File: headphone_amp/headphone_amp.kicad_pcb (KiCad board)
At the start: 2 copper layers, 40 parts, among them J1 Molex_SL_01x02_Male, J2 Molex_SL_01x02_Male, J3 Molex_SL_01x03_Male, J4 Molex_SL_01x03_Male, Q1 PZTA42, Q2 PZTA92, Q3 PZTA42, Q4 PZTA92, U1 NE5532

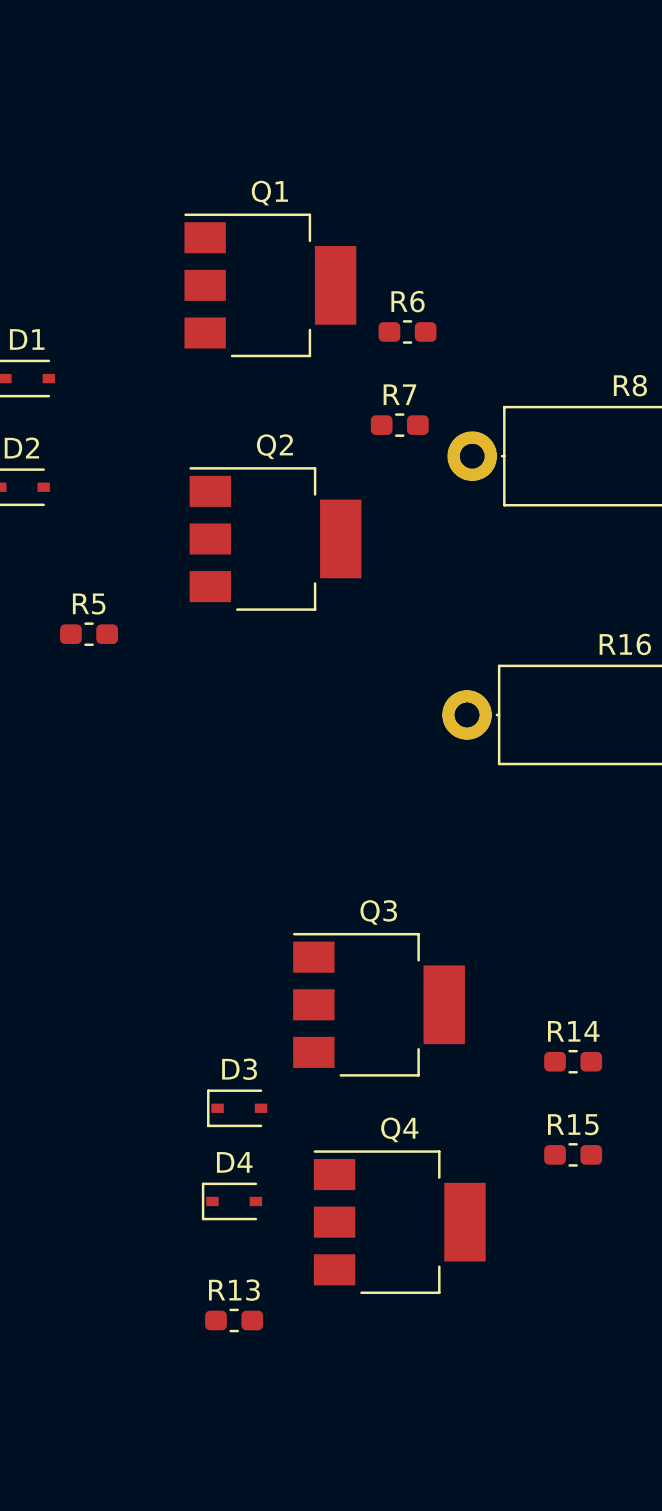
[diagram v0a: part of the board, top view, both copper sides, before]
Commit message: update output transistor symbols/footprints
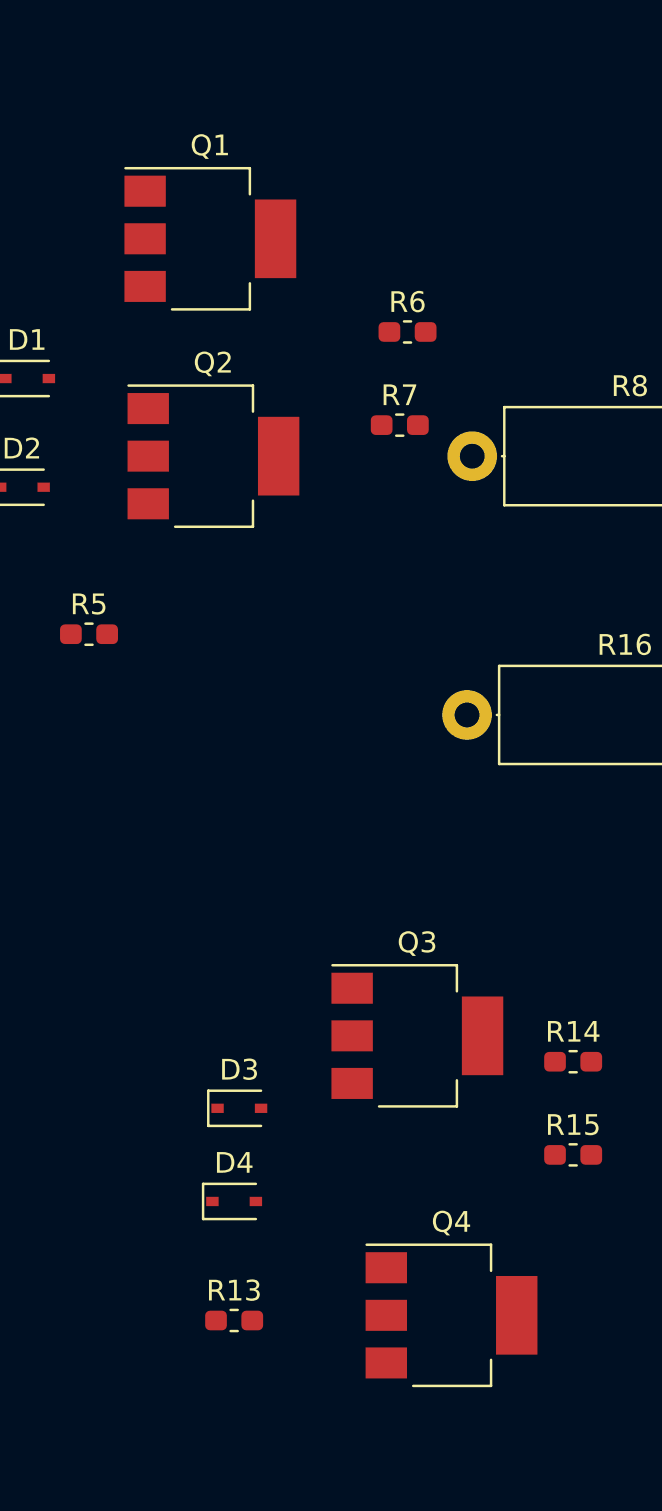
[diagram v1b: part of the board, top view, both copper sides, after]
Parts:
- Q1, Q2, Q3, Q4: footprint Package_TO_SOT_SMD:SOT-223 -> Package_TO_SOT_SMD:SOT-223-3_TabPin2
- moved Q4 5.15 mm to (93.5, 167.0)
- moved Q2 5.00 mm to (82.0, 125.5)
- moved Q1 3.67 mm to (81.8, 115.0)
- moved Q3 2.38 mm to (91.8, 153.5)
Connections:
- Q2 pad 1: Net-(D2-Pad1) -> Net-(Q2-Pad1)
- Q2 pad 2: VEE -> Net-(D2-Pad1)
- Q2 pad 3: Net-(Q2-Pad3) -> VEE
- Q4 pad 1: Net-(D4-Pad1) -> Net-(Q4-Pad1)
- Q4 pad 2: VEE -> Net-(D4-Pad1)
- Q4 pad 3: Net-(Q4-Pad3) -> VEE
- R15 pad 2: Net-(Q4-Pad3) -> Net-(Q4-Pad1)
- R7 pad 2: Net-(Q2-Pad3) -> Net-(Q2-Pad1)

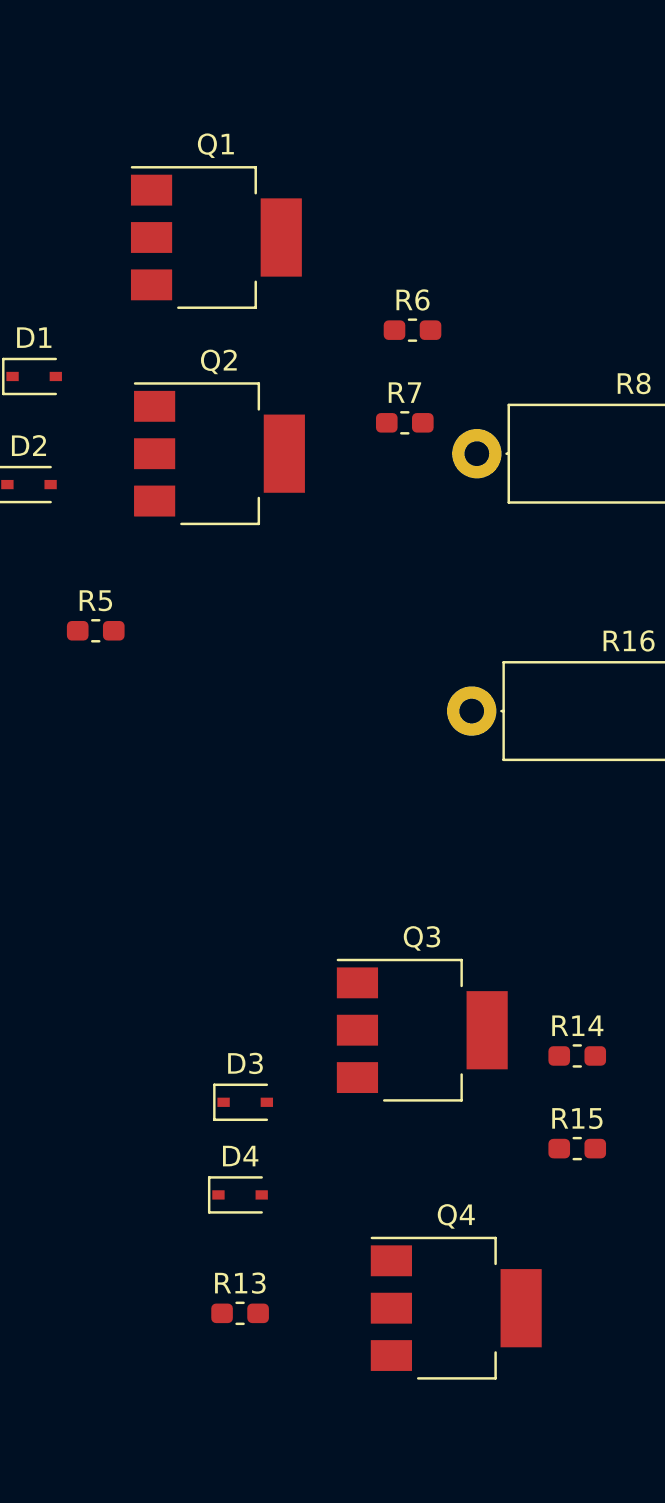
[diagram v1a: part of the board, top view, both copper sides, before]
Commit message: change output transistors to std lib versions (now in upstream)
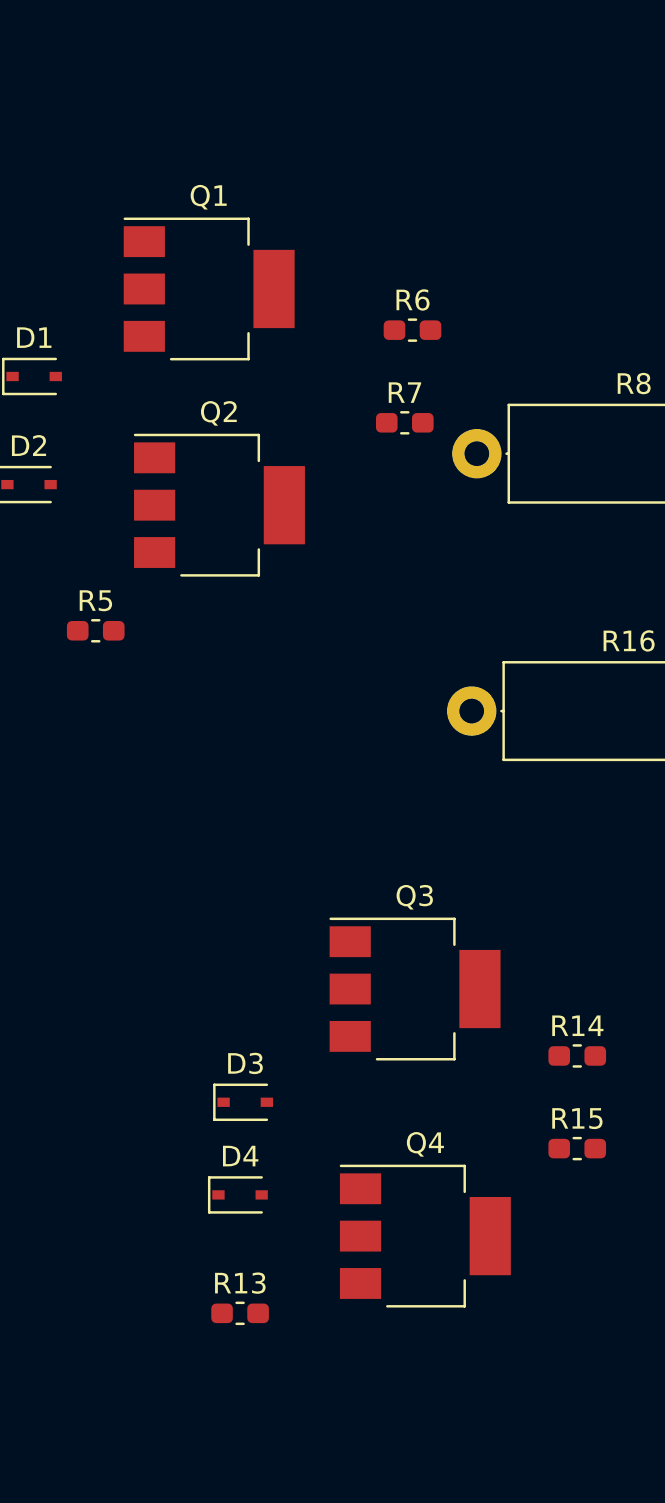
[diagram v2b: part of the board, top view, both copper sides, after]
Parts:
- moved Q4 3.81 mm to (92.0, 163.5)
- moved Q1 2.52 mm to (81.5, 117.5)
- moved Q2 2.50 mm to (82.0, 128.0)
- moved Q3 2.03 mm to (91.5, 151.5)
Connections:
- Q2 pad 1: Net-(Q2-Pad1) -> Net-(D2-Pad1)
- Q2 pad 2: Net-(D2-Pad1) -> VEE
- Q2 pad 3: VEE -> Net-(Q2-Pad3)
- Q4 pad 1: Net-(Q4-Pad1) -> Net-(D4-Pad1)
- Q4 pad 2: Net-(D4-Pad1) -> VEE
- Q4 pad 3: VEE -> Net-(Q4-Pad3)
- R15 pad 2: Net-(Q4-Pad1) -> Net-(Q4-Pad3)
- R7 pad 2: Net-(Q2-Pad1) -> Net-(Q2-Pad3)
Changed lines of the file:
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@@
   (net 24 "Net-(Q1-Pad3)")
   (net 25 "Net-(Q3-Pad3)")
-  (net 26 "Net-(Q2-Pad1)")
-  (net 27 "Net-(Q4-Pad1)")
+  (net 26 "Net-(Q2-Pad3)")
+  (net 27 "Net-(Q4-Pad3)")
   (net_class Default "This is the default net class."
     (clearance 0.2)
@@
     (add_net "Net-(D4-Pad1)")
     (add_net "Net-(Q1-Pad3)")
-    (add_net "Net-(Q2-Pad1)")
+    (add_net "Net-(Q2-Pad3)")
     (add_net "Net-(Q3-Pad3)")
-    (add_net "Net-(Q4-Pad1)")
+    (add_net "Net-(Q4-Pad3)")
     (add_net VCC)
     (add_net VEE)
   )
   (module Package_TO_SOT_SMD:SOT-223-3_TabPin2 (layer F.Cu)
-    (at 93.5 167)
+    (at 92 163.5)
     (descr "module CMS SOT223 4 pins")
     (tags "CMS SOT")
@@
     )
     (pad 1 smd rect (at -3.15 -2.3) (size 2 1.5) (layers F.Cu F.Paste F.Mask)
-      (net 27 "Net-(Q4-Pad1)"))
+      (net 17 "Net-(D4-Pad1)"))
     (pad 3 smd rect (at -3.15 2.3) (size 2 1.5) (layers F.Cu F.Paste F.Mask)
+      (net 27 "Net-(Q4-Pad3)"))
+    (pad 2 smd rect (at -3.15 0) (size 2 1.5) (layers F.Cu F.Paste F.Mask)
       (net 10 VEE))
-    (pad 2 smd rect (at -3.15 0) (size 2 1.5) (layers F.Cu F.Paste F.Mask)
-      (net 17 "Net-(D4-Pad1)"))
     (pad 2 smd rect (at 3.15 0) (size 2 3.8) (layers F.Cu F.Paste F.Mask)
-      (net 17 "Net-(D4-Pad1)"))
+      (net 10 VEE))
     (model ${KISYS3DMOD}/Package_TO_SOT_SMD.3dshapes/SOT-223.wrl
       (at (xyz 0 0 0))
@@
   )
   (module Package_TO_SOT_SMD:SOT-223-3_TabPin2 (layer F.Cu)
-    (at 91.85 153.5)
+    (at 91.5 151.5)
     (descr "module CMS SOT223 4 pins")
     (tags "CMS SOT")
@@
   )
   (module Package_TO_SOT_SMD:SOT-223-3_TabPin2 (layer F.Cu)
-    (at 82 125.5)
+    (at 82 128)
     (descr "module CMS SOT223 4 pins")
     (tags "CMS SOT")
@@
     )
     (pad 1 smd rect (at -3.15 -2.3) (size 2 1.5) (layers F.Cu F.Paste F.Mask)
-      (net 26 "Net-(Q2-Pad1)"))
+      (net 14 "Net-(D2-Pad1)"))
     (pad 3 smd rect (at -3.15 2.3) (size 2 1.5) (layers F.Cu F.Paste F.Mask)
+      (net 26 "Net-(Q2-Pad3)"))
+    (pad 2 smd rect (at -3.15 0) (size 2 1.5) (layers F.Cu F.Paste F.Mask)
       (net 10 VEE))
-    (pad 2 smd rect (at -3.15 0) (size 2 1.5) (layers F.Cu F.Paste F.Mask)
-      (net 14 "Net-(D2-Pad1)"))
     (pad 2 smd rect (at 3.15 0) (size 2 3.8) (layers F.Cu F.Paste F.Mask)
-      (net 14 "Net-(D2-Pad1)"))
+      (net 10 VEE))
     (model ${KISYS3DMOD}/Package_TO_SOT_SMD.3dshapes/SOT-223.wrl
       (at (xyz 0 0 0))
@@
   )
   (module Package_TO_SOT_SMD:SOT-223-3_TabPin2 (layer F.Cu)
-    (at 81.85 115)
+    (at 81.5 117.5)
     (descr "module CMS SOT223 4 pins")
     (tags "CMS SOT")
@@
     (fp_line (start -0.8 0.4) (end -0.8 -0.4) (layer F.Fab) (width 0.1))
     (pad 2 smd roundrect (at 0.875 0) (size 1.05 0.95) (layers F.Cu F.Paste F.Mask) (roundrect_rratio 0.25)
-      (net 27 "Net-(Q4-Pad1)"))
+      (net 27 "Net-(Q4-Pad3)"))
     (pad 1 smd roundrect (at -0.875 0) (size 1.05 0.95) (layers F.Cu F.Paste F.Mask) (roundrect_rratio 0.25)
       (net 7 "Net-(C4-Pad1)"))
@@
     (fp_line (start -0.8 0.4) (end -0.8 -0.4) (layer F.Fab) (width 0.1))
     (pad 2 smd roundrect (at 0.875 0) (size 1.05 0.95) (layers F.Cu F.Paste F.Mask) (roundrect_rratio 0.25)
-      (net 26 "Net-(Q2-Pad1)"))
+      (net 26 "Net-(Q2-Pad3)"))
     (pad 1 smd roundrect (at -0.875 0) (size 1.05 0.95) (layers F.Cu F.Paste F.Mask) (roundrect_rratio 0.25)
       (net 2 "Net-(C1-Pad1)"))

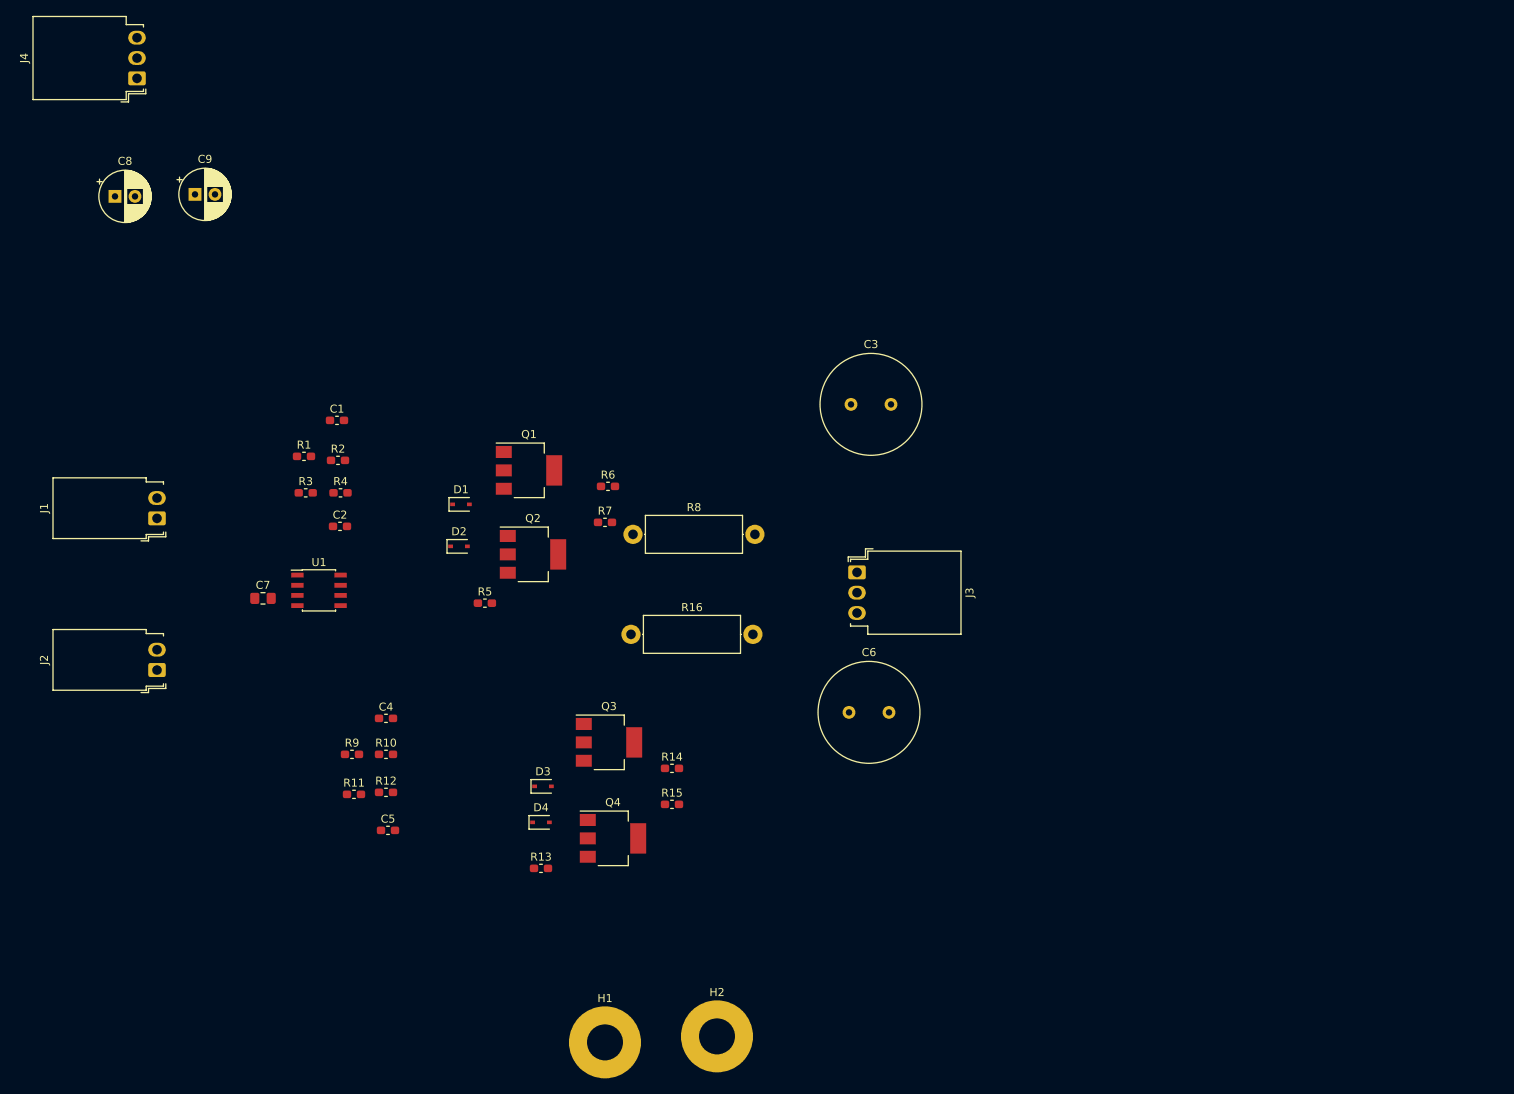
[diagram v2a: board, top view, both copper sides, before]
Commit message: initial layout for headphone amplifier. Still need to finalize mounting orientation and adjust connectors/mounting holes if necessary
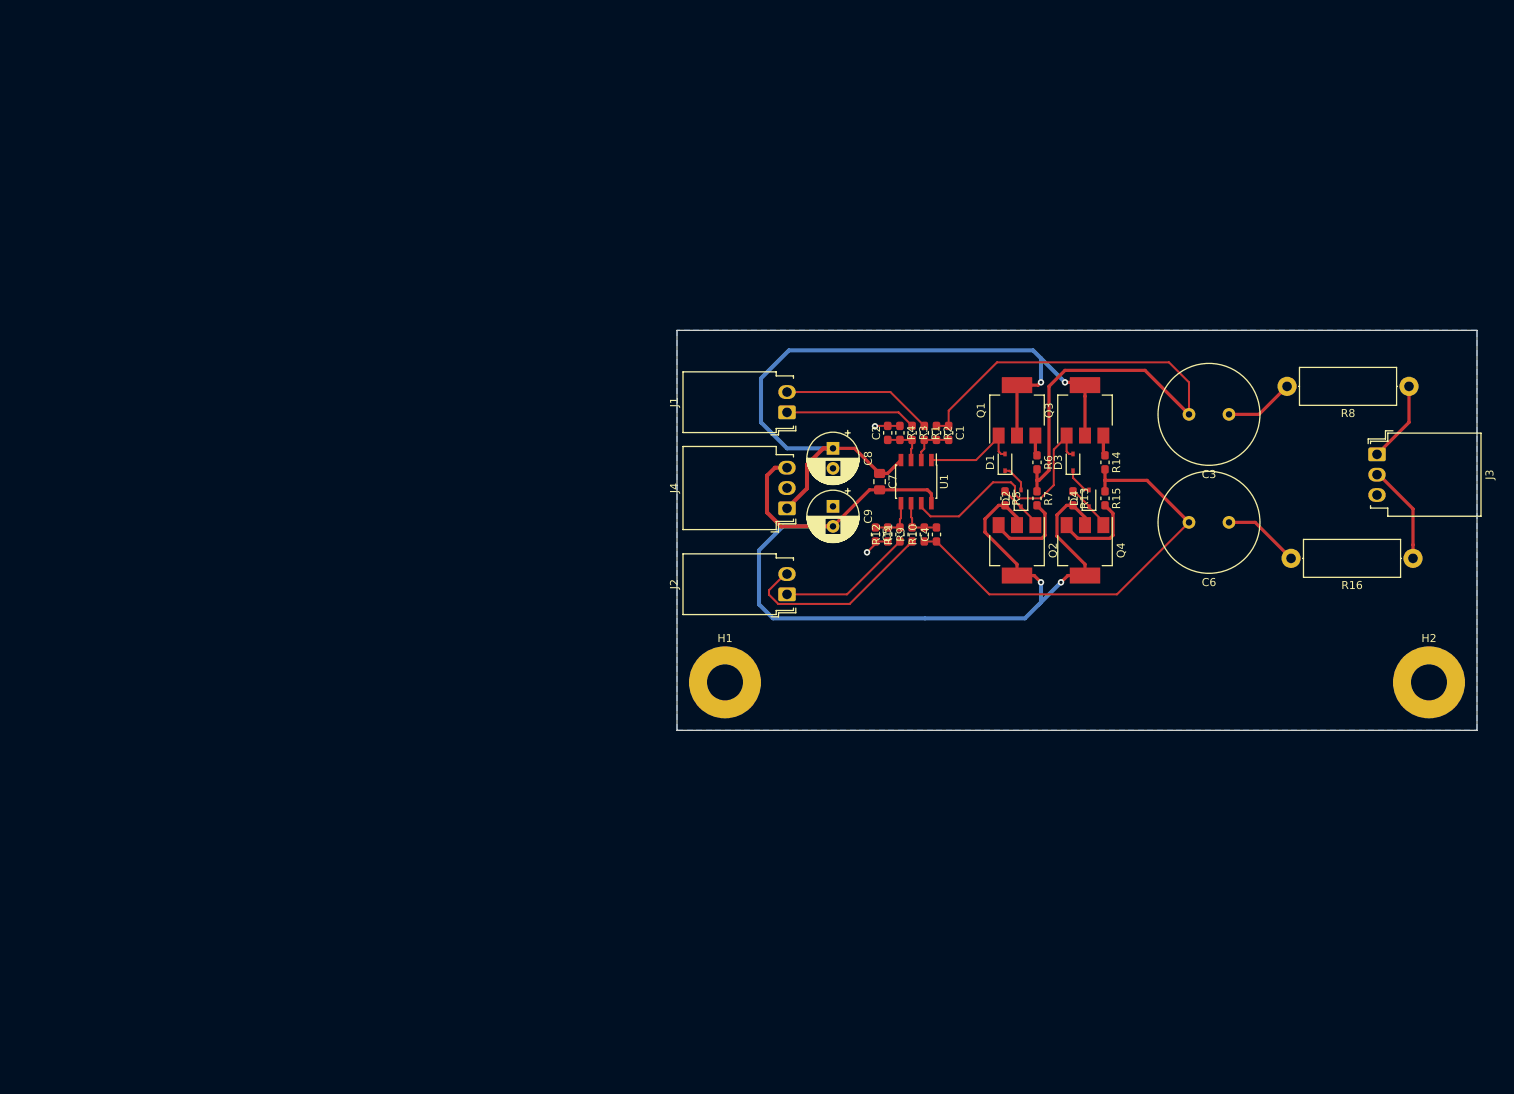
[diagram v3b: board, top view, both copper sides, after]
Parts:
- moved H2 99.4 mm to (194.0, 144.0)
- moved R8 98.7 mm to (191.5, 107.0), turned to 180 degrees
- moved R16 98.2 mm to (192.0, 128.5), turned to 180 degrees
- moved J4 97.4 mm to (113.8, 122.2)
- moved C8 95.1 mm to (119.5, 114.8), turned to 270 degrees
- moved C9 88.8 mm to (119.5, 122.0), turned to 270 degrees
- moved R13 81.0 mm to (149.5, 121.0), turned to 270 degrees
- moved J1 79.9 mm to (113.8, 110.2)
- moved D4 79.6 mm to (151.5, 121.0), turned to 90 degrees
- moved J2 79.3 mm to (113.8, 133.0)
- moved C7 78.4 mm to (125.3, 118.9), turned to 270 degrees
- moved D3 77.6 mm to (149.5, 116.5), turned to 90 degrees
- moved R1 77.6 mm to (130.9, 112.8), turned to 270 degrees
- moved C1 76.5 mm to (134.0, 112.8), turned to 270 degrees
- moved R3 76.2 mm to (129.4, 112.8), turned to 270 degrees
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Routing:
- net VEE: track 0.00 -> 129.6 mm, vias 0 -> 2
- net VCC: track 0.00 -> 99.4 mm, vias 0 -> 2
- net Net-(C1-Pad1): track 0.00 -> 76.9 mm
- net Net-(C4-Pad1): track 0.00 -> 55.0 mm
- net Net-(D3-Pad2): track 0.00 -> 31.2 mm
- net /right_cold: track 0.00 -> 25.2 mm
- net /left_cold: track 0.00 -> 18.9 mm
- net /right_hot: track 0.00 -> 16.9 mm
- net /left_hot: track 0.00 -> 16.3 mm
- net Net-(D1-Pad2): track 0.00 -> 12.7 mm
- net /right_out: track 0.00 -> 12.5 mm
- net Net-(Q2-Pad3): track 0.00 -> 10.9 mm
- net Net-(Q4-Pad3): track 0.00 -> 10.9 mm
- net /left_out: track 0.00 -> 10.2 mm
- net Net-(C6-Pad1): track 0.00 -> 9.62 mm
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- added copper zone on B.Cu, net GNDA
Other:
- board outline added: 100 x 50 mm
- net class Audio added: clearance 0.2, trace_width 0.254, via_dia 0.8, via_drill 0.4
- net class Default: trace_width 0.25 -> 0.2
- net class Output added: clearance 0.2, trace_width 0.4064, via_dia 0.8, via_drill 0.4
- net class Power added: clearance 0.2, trace_width 0.4064, via_dia 0.8, via_drill 0.4
- board text added: "TODO check height of all components, especially output caps choose orientation and rearrange connectors?"
